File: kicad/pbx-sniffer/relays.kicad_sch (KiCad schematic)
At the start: 8 parts, among them K1 Relay_SPST-NO, K4 Relay_SPDT, Q3 PMOS, Q4 NMOS

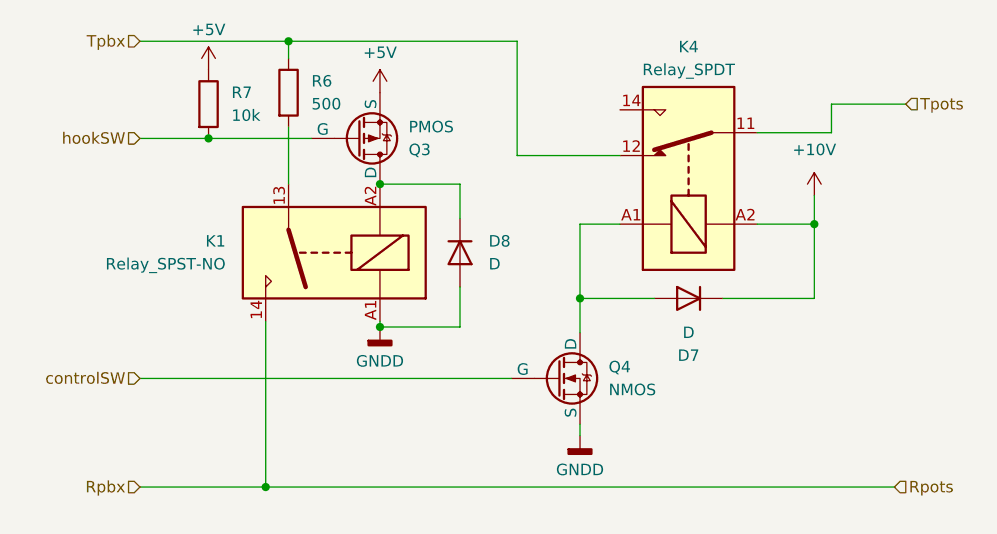
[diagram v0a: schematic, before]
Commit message: fixed minor mistake on relay sch
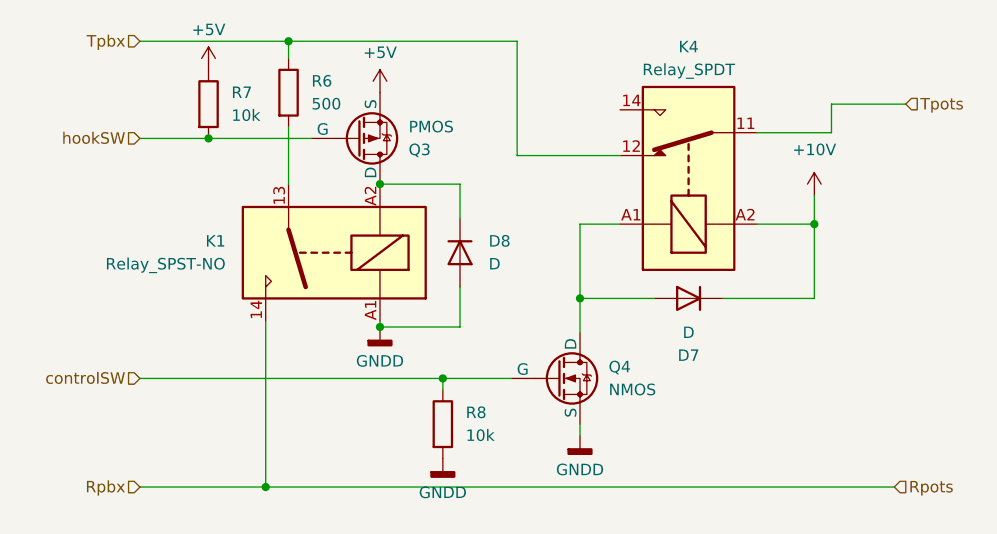
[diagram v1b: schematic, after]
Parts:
- added R8: 10k, symbol Device:R
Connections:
- net GNDD: now also R8.2
- net controlSW: now also R8.1
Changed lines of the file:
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@@
+	)
+	(junction
+		(at 77.47 67.945)
+		(diameter 0)
+		(color 0 0 0 0)
 	)
 	(junction
@@
 	(wire
 		(pts
+			(xy 77.47 67.945) (xy 77.47 69.215)
+		)
+		(stroke
+			(width 0)
+			(type default)
+		)
+	)
+	(wire
+		(pts
 			(xy 118.745 47.625) (xy 118.745 50.8)
 		)
@@
 	(wire
 		(pts
+			(xy 77.47 67.945) (xy 85.09 67.945)
+		)
+		(stroke
+			(width 0)
+			(type default)
+		)
+	)
+	(wire
+		(pts
 			(xy 57.785 61.595) (xy 57.785 80.01)
 		)
@@
 	(wire
 		(pts
-			(xy 43.815 67.945) (xy 85.09 67.945)
+			(xy 43.815 67.945) (xy 77.47 67.945)
 		)
 		(stroke
@@
 	)
 	(symbol
+		(lib_id "Device:R")
+		(at 77.47 73.025 0)
+		(unit 1)
+		(exclude_from_sim no)
+		(in_bom yes)
+		(on_board yes)
+		(dnp no)
+		(fields_autoplaced yes)
+		(property "Reference" "R8"
+			(at 80.01 71.7549 0)
+			(effects
+				(font
+					(size 1.27 1.27)
+				)
+				(justify left)
+			)
+		)
+		(property "Value" "10k"
+			(at 80.01 74.2949 0)
+			(effects
+				(font
+					(size 1.27 1.27)
+				)
+				(justify left)
+			)
+		)
+		(property "Footprint" ""
+			(at 75.692 73.025 90)
+			(effects
+				(font
+					(size 1.27 1.27)
+				)
+				(hide yes)
+			)
+		)
+		(property "Datasheet" "~"
+			(at 77.47 73.025 0)
+			(effects
+				(font
+					(size 1.27 1.27)
+				)
+				(hide yes)
+			)
+		)
+		(property "Description" "Resistor"
+			(at 77.47 73.025 0)
+			(effects
+				(font
+					(size 1.27 1.27)
+				)
+				(hide yes)
+			)
+		)
+		(pin "1"
+		)
+		(pin "2"
+		)
+		(instances
+			(project "pbx-sniffer"
+				(path "/4a5b9b8a-323a-4796-bf73-ccba532d2e31/992e173b-e387-457c-8c0b-8a825a1cd866"
+					(reference "R8")
+					(unit 1)
+				)
+			)
+		)
+	)
+	(symbol
 		(lib_id "power:GNDD")
 		(at 70.485 62.23 0)
@@
 					(unit 1)
 				)
+			)
+		)
+	)
+	(symbol
+		(lib_id "power:GNDD")
+		(at 77.47 76.835 0)
+		(unit 1)
+		(exclude_from_sim no)
+		(in_bom yes)
+		(on_board yes)
+		(dnp no)
+		(fields_autoplaced yes)
+		(property "Reference" "#PWR045"
+			(at 77.47 83.185 0)
+			(effects
+				(font
+					(size 1.27 1.27)
+				)
+				(hide yes)
+			)
+		)
+		(property "Value" "GNDD"
+			(at 77.47 80.645 0)
+			(effects
+				(font
+					(size 1.27 1.27)
+				)
+			)
+		)
+		(property "Footprint" ""
+			(at 77.47 76.835 0)
+			(effects
+				(font
+					(size 1.27 1.27)
+				)
+				(hide yes)
+			)
+		)
+		(property "Datasheet" ""
+			(at 77.47 76.835 0)
+			(effects
+				(font
+					(size 1.27 1.27)
+				)
+				(hide yes)
+			)
+		)
+		(property "Description" "Power symbol creates a global label with name \"GNDD\" , digital ground"
+			(at 77.47 76.835 0)
+			(effects
+				(font
+					(size 1.27 1.27)
+				)
+				(hide yes)
+			)
+		)
+		(pin "1"
+		)
+		(instances
+			(project "pbx-sniffer"
+				(path "/4a5b9b8a-323a-4796-bf73-ccba532d2e31/992e173b-e387-457c-8c0b-8a825a1cd866"
+					(reference "#PWR045")
+					(unit 1)
+				)

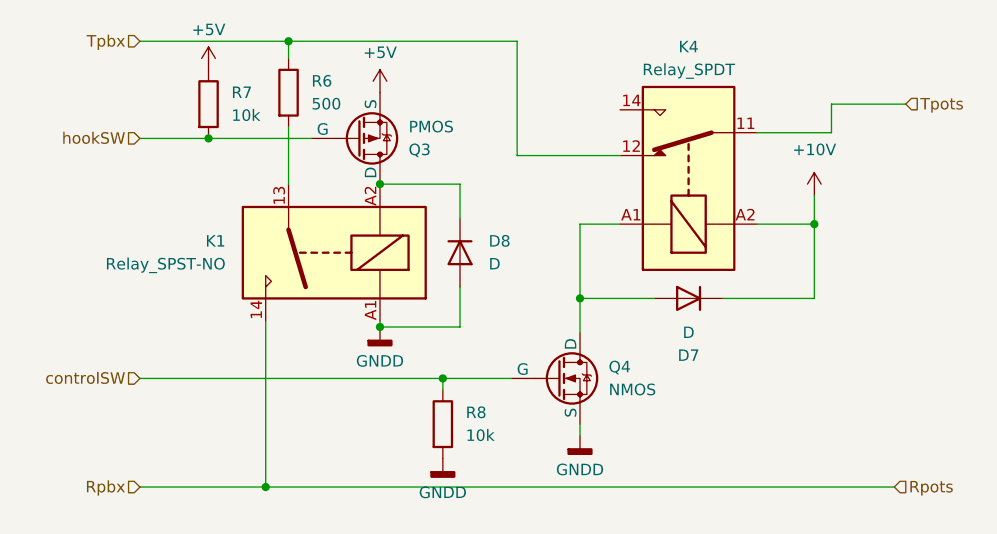
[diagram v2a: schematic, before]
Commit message: added adc sheet
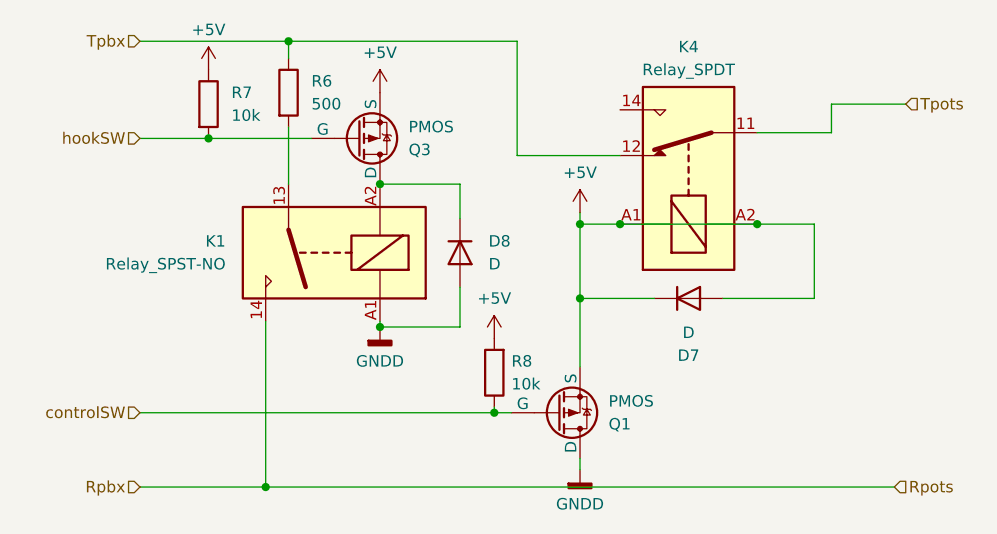
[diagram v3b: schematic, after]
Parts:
- removed Q4: NMOS, symbol Simulation_SPICE:NMOS
- added Q1: PMOS, symbol Simulation_SPICE:PMOS
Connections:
- net +10V is gone; now on net +5V: D7.1 (K), K4.A2
- net +5V: now also D7.2 (A), K4.A1, R8.2, Q1.3 (S)
- net GNDD: now also Q1.1 (D); no longer R8.2
- net controlSW: now also Q1.2 (G)
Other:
- moved on the sheet: R8

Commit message: updated multiplexer with busses, added ADCs, fixed relay sch
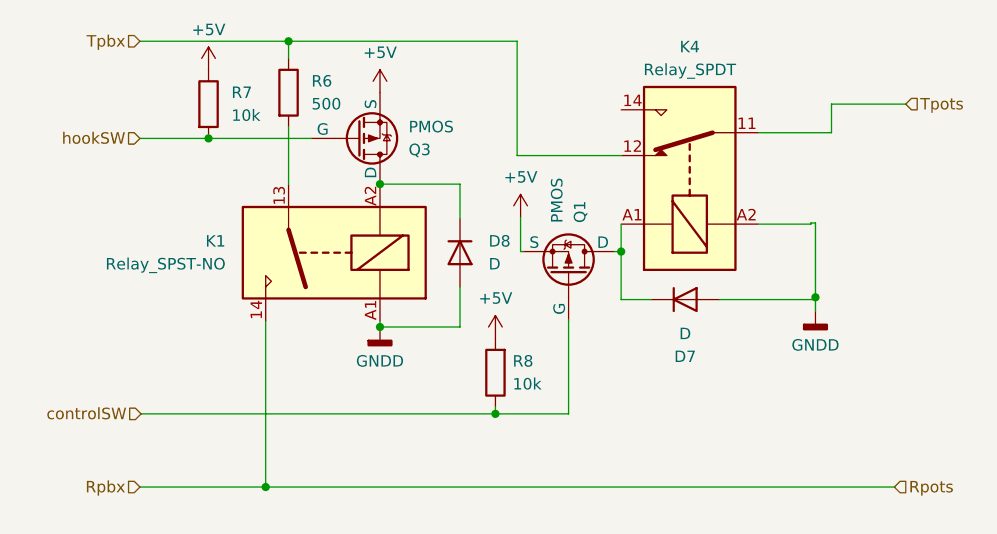
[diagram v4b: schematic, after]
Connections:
- net +5V: no longer D7.1 (K), D7.2 (A), K4.A1, K4.A2
- net GNDD: now also D7.2 (A), K4.A2; no longer Q1.1 (D)
- new net: D7.1 (K), K4.A1, Q1.1 (D)
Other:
- moved on the sheet: Q1

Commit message: assigned footprints, added components to pcb
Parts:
- D7, D8: footprint (none) -> Diode_THT:D_A-405_P12.70mm_Horizontal
- K1: footprint (none) -> Relay_THT:Relay_StandexMeder_DIP_HighProfile
- K4: footprint (none) -> Relay_THT:Relay_SPDT_Panasonic_JW1_FormC
- Q1, Q3: footprint (none) -> Package_TO_SOT_THT:TO-92_HandSolder
- R6, R7, R8: footprint (none) -> Resistor_THT:R_Axial_DIN0207_L6.3mm_D2.5mm_P10.16mm_Horizontal
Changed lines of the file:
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@@
 			)
 		)
-		(property "Footprint" ""
+		(property "Footprint" "Resistor_THT:R_Axial_DIN0207_L6.3mm_D2.5mm_P10.16mm_Horizontal"
 			(at 58.547 36.195 90)
 			(effects
@@
 			)
 		)
-		(property "Footprint" ""
+		(property "Footprint" "Relay_THT:Relay_SPDT_Panasonic_JW1_FormC"
 			(at 106.172 34.29 0)
 			(effects
@@
 			)
 		)
-		(property "Footprint" ""
+		(property "Footprint" "Diode_THT:D_A-405_P12.70mm_Horizontal"
 			(at 79.375 53.975 0)
 			(effects
@@
 			)
 		)
-		(property "Footprint" ""
+		(property "Footprint" "Resistor_THT:R_Axial_DIN0207_L6.3mm_D2.5mm_P10.16mm_Horizontal"
 			(at 85.09 67.31 90)
 			(effects
@@
 			)
 		)
-		(property "Footprint" ""
+		(property "Footprint" "Package_TO_SOT_THT:TO-92_HandSolder"
 			(at 73.025 43.815 0)
 			(effects
@@
 			)
 		)
-		(property "Footprint" ""
+		(property "Footprint" "Diode_THT:D_A-405_P12.70mm_Horizontal"
 			(at 104.394 59.182 0)
 			(effects
@@
 			)
 		)
-		(property "Footprint" ""
+		(property "Footprint" "Relay_THT:Relay_StandexMeder_DIP_HighProfile"
 			(at 53.975 52.705 0)
 			(effects
@@
 			)
 		)
-		(property "Footprint" ""
+		(property "Footprint" "Package_TO_SOT_THT:TO-92_HandSolder"
 			(at 93.98 51.308 0)
 			(effects
@@
 			)
 		)
-		(property "Footprint" ""
+		(property "Footprint" "Resistor_THT:R_Axial_DIN0207_L6.3mm_D2.5mm_P10.16mm_Horizontal"
 			(at 49.657 37.465 90)
 			(effects

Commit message: commenced placement on pcb
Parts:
- K1: footprint Relay_THT:Relay_StandexMeder_DIP_HighProfile -> Relay_THT:Relay_SPST_StandexMeder_SIL_Form1A
- renumbered D8 to D2, D7 to D3, K4 to K2, Q3 to Q1, Q1 to Q2, R7 to R3, R6 to R4, R8 to R5
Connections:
- net GNDD: now also K1.5, K2.8; no longer K1.A1, K2.A2
- net Rpbx: now also K1.7; no longer K1.14
- net Tpbx: now also K2.2; no longer K2.12
- net Tpots: now also K2.6; no longer K2.11
- net at R4.2: now also K1.1; no longer K1.13
- net at D3.1 (K), Q2.1 (D): now also K2.1; no longer K2.A1
- net at D2.1 (K), Q1.1 (D): now also K1.3; no longer K1.A2

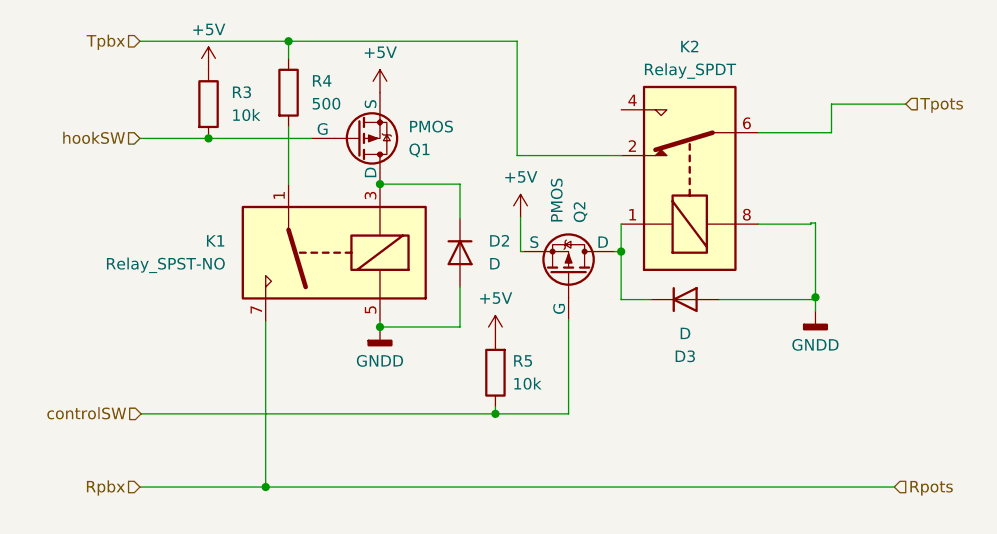
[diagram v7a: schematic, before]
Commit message: add SPDT relay footprint and update symbol for it
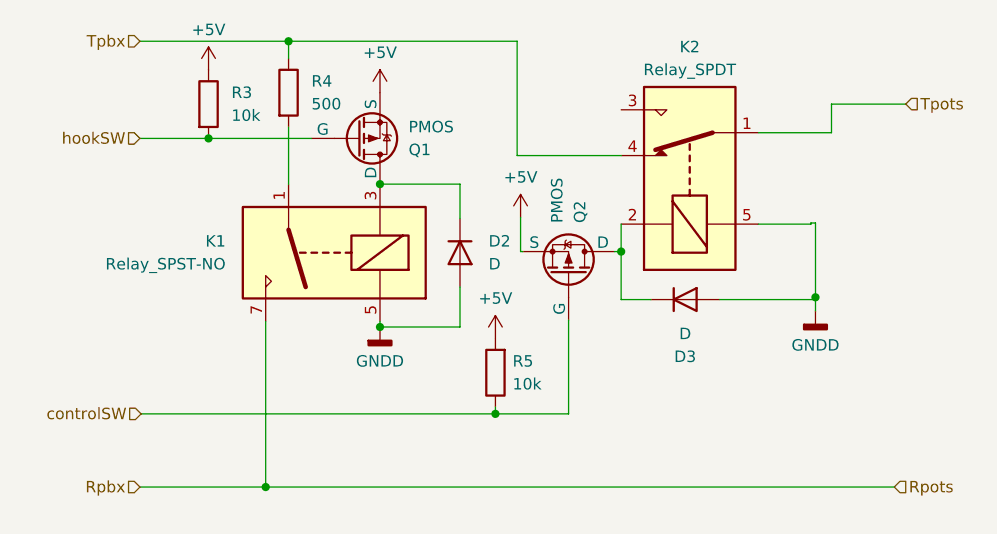
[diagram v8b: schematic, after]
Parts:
- K2: footprint Relay_THT:Relay_SPDT_Panasonic_JW1_FormC -> Phones:K_AZ943-1C_AMZ
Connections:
- net GNDD: now also K2.5; no longer K2.8
- net Tpbx: now also K2.4; no longer K2.2
- net Tpots: now also K2.1; no longer K2.6
- net at D3.1 (K), Q2.1 (D): now also K2.2; no longer K2.1
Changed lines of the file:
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@@
 			)
 		)
-		(property "Footprint" "Relay_THT:Relay_SPDT_Panasonic_JW1_FormC"
+		(property "Footprint" "Phones:K_AZ943-1C_AMZ"
 			(at 106.172 34.29 0)
 			(effects
@@
 		(pin "4"
 		)
-		(pin "8"
+		(pin "3"
 		)
-		(pin "6"
+		(pin "5"
 		)
 		(pin "2"
